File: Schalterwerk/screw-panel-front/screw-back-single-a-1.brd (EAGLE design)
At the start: 50 x 66 mm, 12 parts, among them J1 M4-SCREW-HOLEHEAD, J2 M4-SCREW-HOLEHEAD, J3 M4-SCREW-HOLEHEAD, J4 M4-SCREW-HOLEHEAD, J5 M4-SCREW-HOLEHEAD, J6 M4-SCREW-HOLEHEAD, J7 M4-SCREW-HOLEHEAD, J8 M4-SCREW-HOLEHEAD

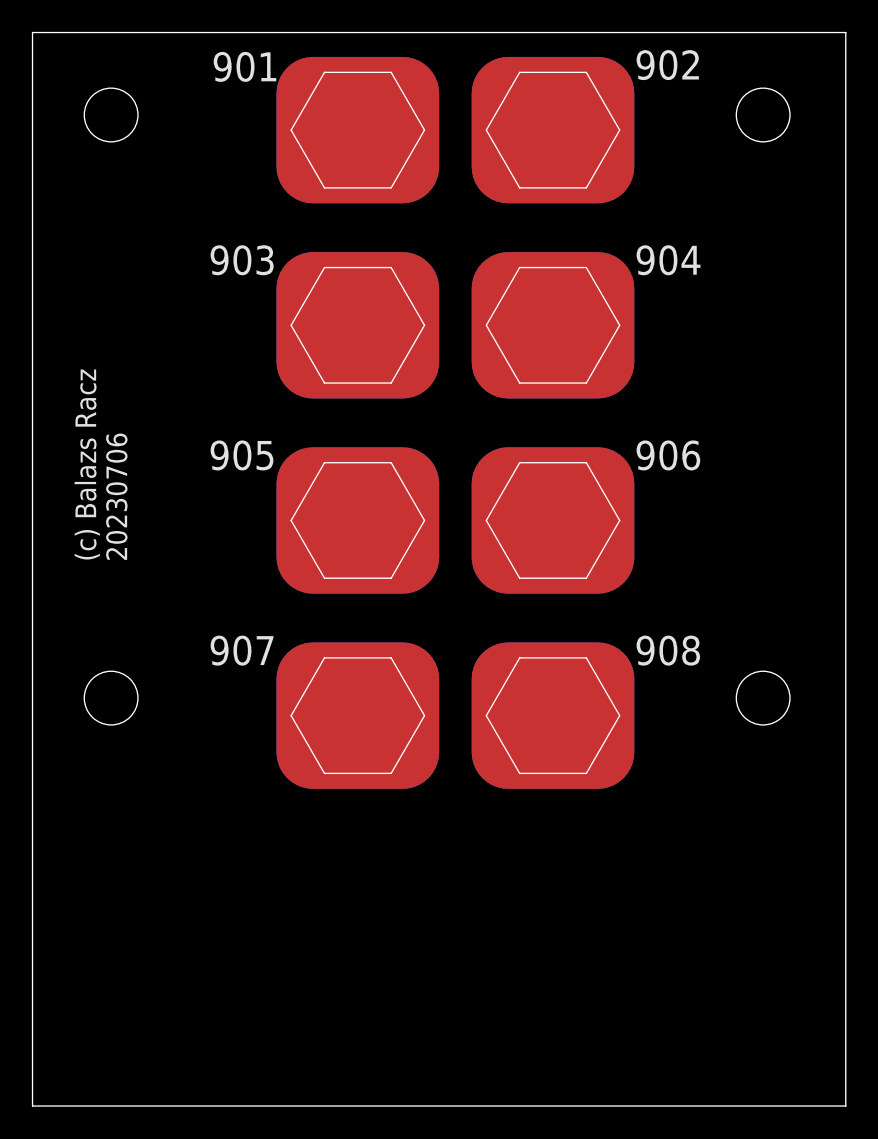
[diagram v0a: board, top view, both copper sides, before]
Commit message: Adds alignment holes.
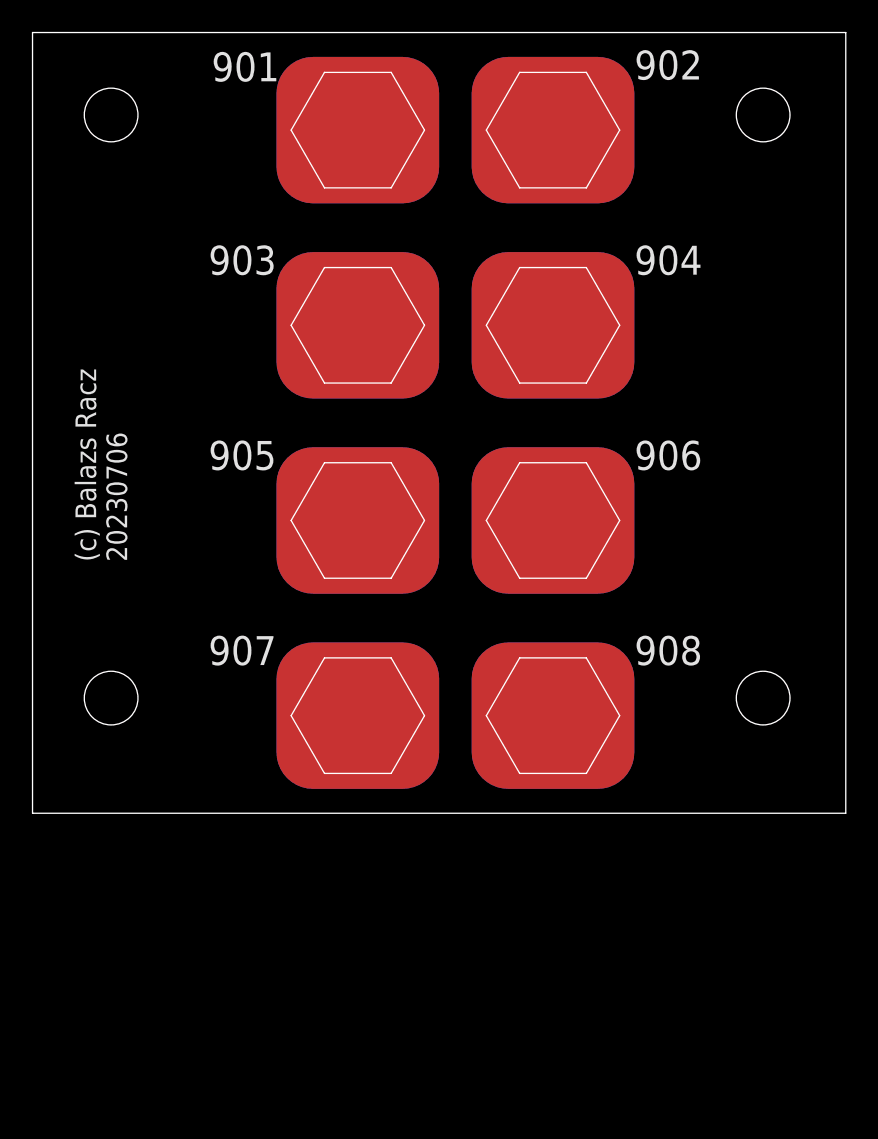
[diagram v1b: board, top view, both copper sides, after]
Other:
- board size 50 x 66 mm -> 50 x 48 mm
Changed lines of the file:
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@@
 <layer number="25" name="tNames" color="7" fill="1" visible="yes" active="yes"/>
 <layer number="26" name="bNames" color="7" fill="1" visible="yes" active="yes"/>
-<layer number="27" name="tValues" color="7" fill="1" visible="yes" active="yes"/>
+<layer number="27" name="tValues" color="7" fill="1" visible="no" active="yes"/>
 <layer number="28" name="bValues" color="7" fill="1" visible="no" active="yes"/>
 <layer number="29" name="tStop" color="7" fill="3" visible="no" active="yes"/>
@@
 <layer number="44" name="Drills" color="7" fill="1" visible="no" active="yes"/>
 <layer number="45" name="Holes" color="7" fill="1" visible="no" active="yes"/>
-<layer number="46" name="Milling" color="3" fill="1" visible="yes" active="yes"/>
+<layer number="46" name="Milling" color="3" fill="1" visible="no" active="yes"/>
 <layer number="47" name="Measures" color="7" fill="1" visible="no" active="yes"/>
 <layer number="48" name="Document" color="7" fill="1" visible="no" active="yes"/>
@@
 <board>
 <plain>
-<wire x1="0" y1="0" x2="50" y2="0" width="0" layer="20"/>
-<wire x1="50" y1="0" x2="50" y2="66" width="0" layer="20"/>
+<wire x1="0" y1="18" x2="50" y2="18" width="0" layer="20"/>
+<wire x1="50" y1="18" x2="50" y2="66" width="0" layer="20"/>
 <wire x1="50" y1="66" x2="0" y2="66" width="0" layer="20"/>
-<wire x1="0" y1="66" x2="0" y2="0" width="0" layer="20"/>
+<wire x1="0" y1="66" x2="0" y2="18" width="0" layer="20"/>
 <text x="5.816" y="33.464" size="1.27" layer="25" font="vector" ratio="10" rot="R90">(c) Balazs Racz
 20230706</text>
